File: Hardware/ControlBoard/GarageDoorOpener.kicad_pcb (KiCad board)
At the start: 2 copper layers, 24 parts, among them J1 Conn_01x02, J2 Conn_01x02, J3 Conn_01x02, J4 Conn_01x02, Q1 DMG1012T-7, U1 RAC15-05SK, U2 CPC1002N

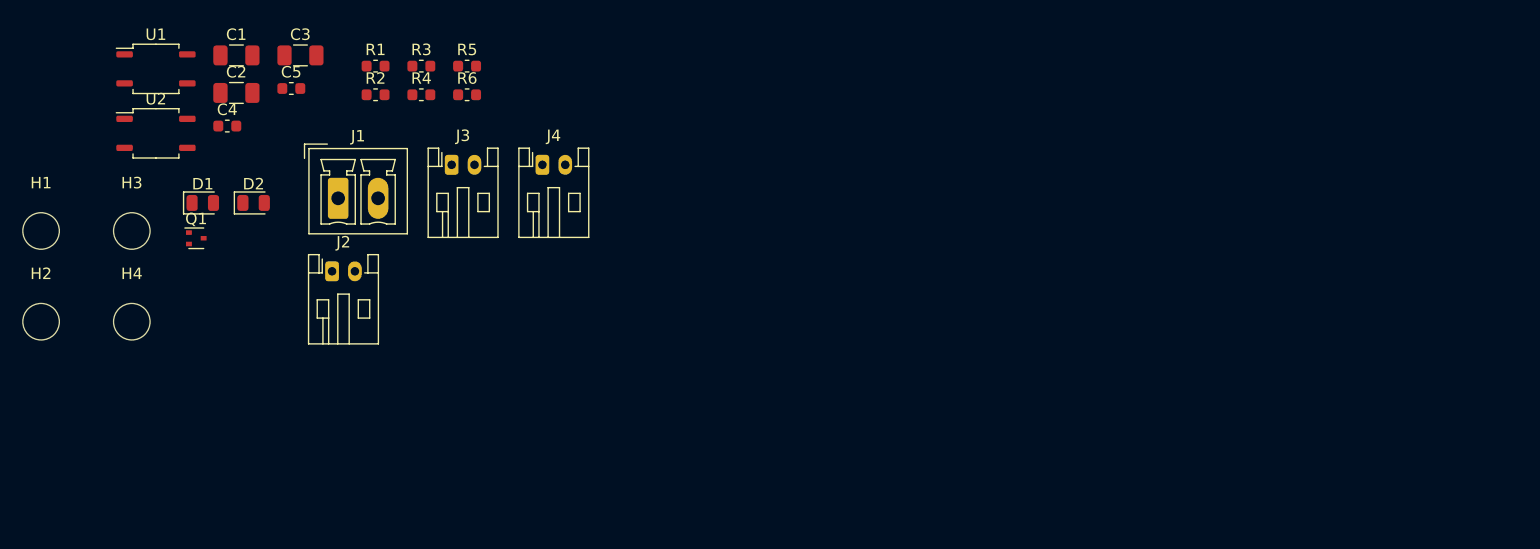
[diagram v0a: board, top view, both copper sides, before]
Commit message: Schematics done, PCBs have components dropped in and BoM finished
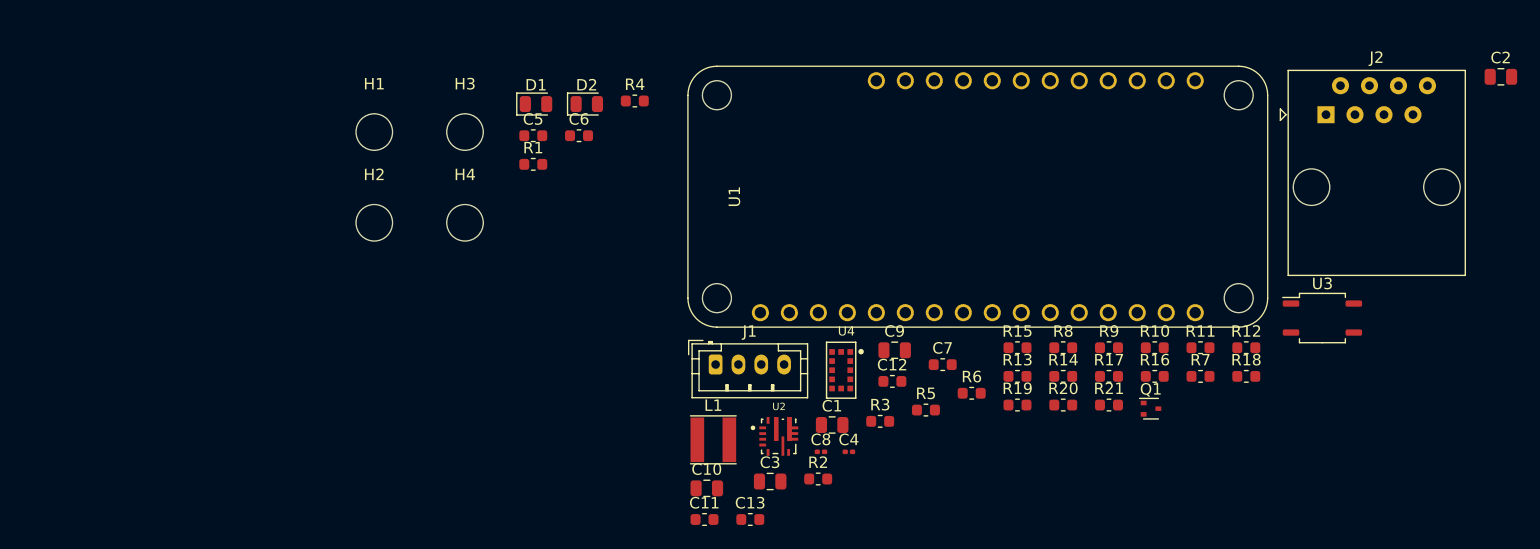
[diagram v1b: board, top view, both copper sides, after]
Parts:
- removed J3, J4: Conn_01x02, Connector_JST:JST_PH_S2B-PH-K_1x02_P2.00mm_Horizontal
- added C10: 22uF 10V, Capacitor_SMD:C_0805_2012Metric, F.Cu at (201.1, 131.0)
- added C11: 4.7uF 10V, Capacitor_SMD:C_0603_1608Metric, F.Cu at (200.9, 133.7)
- added C12: 0.1uF 16V, Capacitor_SMD:C_0603_1608Metric, F.Cu at (217.3, 121.6)
- added C13: 4.7uF 10V, Capacitor_SMD:C_0603_1608Metric, F.Cu at (204.9, 133.7)
- added C6: 1uF 10V, Capacitor_SMD:C_0603_1608Metric, F.Cu at (189.9, 100.1)
- added C7: 0.1uF 16V, Capacitor_SMD:C_0603_1608Metric, F.Cu at (221.8, 120.2)
- added C8: 100pF 10V, Capacitor_SMD:C_0201_0603Metric, F.Cu at (211.1, 127.8)
- added C9: 22uF 10V, Capacitor_SMD:C_0805_2012Metric, F.Cu at (217.5, 118.9)
- added L1: 3.3uH, Inductor_SMD:L_Taiyo-Yuden_NR-40xx, F.Cu at (201.7, 126.8)
- added R10: 73.2K, Resistor_SMD:R_0603_1608Metric, F.Cu at (240.3, 118.7)
- added R11: 10K, Resistor_SMD:R_0603_1608Metric, F.Cu at (244.3, 118.7)
- added R12: 4.7K, Resistor_SMD:R_0603_1608Metric, F.Cu at (248.4, 118.7)
- added R13: 4.7K, Resistor_SMD:R_0603_1608Metric, F.Cu at (228.3, 121.2)
- added R14: 10K, Resistor_SMD:R_0603_1608Metric, F.Cu at (232.3, 121.2)
- added R15: 10K, Resistor_SMD:R_0603_1608Metric, F.Cu at (228.3, 118.7)
- added R16: 0, Resistor_SMD:R_0603_1608Metric, F.Cu at (240.3, 121.2)
- added R17: 0, Resistor_SMD:R_0603_1608Metric, F.Cu at (236.3, 121.2)
- added R18: 0, Resistor_SMD:R_0603_1608Metric, F.Cu at (248.4, 121.2)
- added R19: 0, Resistor_SMD:R_0603_1608Metric, F.Cu at (228.3, 123.7)
- added R20: 0, Resistor_SMD:R_0603_1608Metric, F.Cu at (232.3, 123.7)
- added R21: 0, Resistor_SMD:R_0603_1608Metric, F.Cu at (236.3, 123.7)
- added R7: 10K, Resistor_SMD:R_0603_1608Metric, F.Cu at (244.3, 121.2)
- added R8: 20K, Resistor_SMD:R_0603_1608Metric, F.Cu at (232.3, 118.7)
- added R9: 10K, Resistor_SMD:R_0603_1608Metric, F.Cu at (236.3, 118.7)
- added U3: CPC1002N, Package_SO:SOP-4_3.8x4.1mm_P2.54mm, F.Cu at (255.0, 116.1)
- added U4: VL53L1X, Global_Parts:VL53L1CXV0FY_1, F.Cu at (212.9, 120.7)
- C1, C2, C3: value 47uF 10V -> 4.7uF 50V; footprint Capacitor_SMD:C_1206_3216Metric -> Capacitor_SMD:C_0805_2012Metric
- C4: value 1uF 10V -> 0.1uF 50V; footprint Capacitor_SMD:C_0603_1608Metric -> Capacitor_SMD:C_0201_0603Metric
- D1: value LED -> GREEN_LED
- D2: value LED -> RED_LED
- J1: value Conn_01x02 -> Conn_01x04; footprint Connector_Phoenix_MC:PhoenixContact_MCV_1,5_2-G-3.5_1x02_P3.50mm_Vertical -> Connector_JST:JST_PH_B4B-PH-K_1x04_P2.00mm_Vertical
- J2: value Conn_01x02 -> RJ45; footprint Connector_JST:JST_PH_S2B-PH-K_1x02_P2.00mm_Horizontal -> Connector_RJ:RJ45_Amphenol_54602-x08_Horizontal
- R1: value 1K -> 649
- R2: value 1K -> 10K
- R3: value 10K -> 649
- R4: value 649 -> 1K
- U1: value RAC15-05SK -> Argon/Boron; footprint Package_SO:SOP-4_3.8x4.1mm_P2.54mm -> Global_Parts:ParticleBoron
- U2: value CPC1002N -> TPS56637; footprint Package_SO:SOP-4_3.8x4.1mm_P2.54mm -> Global_Parts:TPS56637RPAR
- moved C2 110.8 mm to (270.7, 94.9)
- moved J2 88.2 mm to (255.3, 98.3)
- moved Q1 85.0 mm to (240.0, 124.0)
- moved U1 70.4 mm to (222.3, 105.4)
- moved C4 61.5 mm to (213.5, 127.8)
- moved C1 61.4 mm to (212.1, 125.5)
- moved U2 60.7 mm to (207.4, 126.5)
- moved C3 55.6 mm to (206.6, 130.4)
- moved R6 51.4 mm to (224.3, 122.7)
- moved R2 51.4 mm to (210.8, 130.2)
- moved R3 50.8 mm to (216.3, 125.1)
- moved R5 50.2 mm to (220.3, 124.1)
- moved J1 36.1 mm to (201.9, 120.2)
- moved D2 30.5 mm to (190.6, 97.3)
- moved D1 30.5 mm to (186.1, 97.3)
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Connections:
- C1 pad 1: +5V -> +24V
- C2 pad 1: +5V -> +24V
- C3 pad 1: +5V -> +24V
- C4 pad 1: +3V3 -> +24V
- J1 pad 1: Net-(J1-Pad1) -> +5V
- J1 pad 2: Net-(J1-Pad2) -> /LED_STRIP_CLK
- J2 pad 1: Net-(J2-Pad1) -> +24V
- J2 pad 2: Net-(J2-Pad2) -> GND
- Q1 pad 1: /RELAY_CTRL -> /RELAY_CTRL1
- R2 pad 1: /STATUS_LED -> GND
- R2 pad 2: Net-(D2-Pad2) -> /RELAY_CTRL1
- R3 pad 1: GND -> Net-(R3-Pad1)
- R3 pad 2: /RELAY_CTRL -> +3V3
- R4 pad 1: Net-(R4-Pad1) -> /STATUS_LED
- R4 pad 2: +3V3 -> Net-(D2-Pad2)
- R5 pad 1: +3V3 -> +24V
- R5 pad 2: /REED_SW1 -> Net-(R5-Pad2)
- R6 pad 1: +3V3 -> +5V
- R6 pad 2: /REED_SW2 -> Net-(R6-Pad2)
- U1 pad 1: Net-(J1-Pad1) -> Net-(U1-Pad1)
- U1 pad 2: (no net) -> +3V3
- U1 pad 3: (no net) -> Net-(U1-Pad3)
- U1 pad 4: (no net) -> GND
- U2 pad 1: Net-(R4-Pad1) -> Net-(R5-Pad2)
- U2 pad 2: Net-(Q1-Pad3) -> Net-(C8-Pad1)
- U2 pad 3: Net-(J2-Pad2) -> GND
- U2 pad 4: Net-(J2-Pad1) -> Net-(R6-Pad2)

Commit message: working on the PCB for the control board
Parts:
- C4, C8: footprint Capacitor_SMD:C_0201_0603Metric -> Capacitor_SMD:C_0603_1608Metric
- moved C2 160.3 mm to (110.6, 85.6), turned to 180 degrees
- moved J2 160.2 mm to (98.2, 66.9), turned to 270 degrees
- moved R18 150.8 mm to (105.7, 72.4)
- moved R16 144.3 mm to (105.7, 69.3)
- moved U3 142.2 mm to (120.6, 69.6), turned to 180 degrees
- moved R11 139.0 mm to (107.3, 95.7), turned to 270 degrees
- moved R17 137.0 mm to (108.9, 70.9)
- moved R21 135.7 mm to (108.9, 77.0)
- moved R20 135.5 mm to (105.7, 75.4)
- moved R10 134.5 mm to (107.3, 98.9), turned to 270 degrees
- moved R19 129.3 mm to (108.9, 73.9)
- moved R8 128.3 mm to (105.6, 98.9), turned to 270 degrees
- moved Q1 127.1 mm to (125.8, 68.3), turned to 180 degrees
- moved R6 117.9 mm to (109.7, 94.8), turned to 180 degrees
- moved R12 117.9 mm to (130.5, 116.0)
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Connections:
- U3 pad 3: /Relay_Ouput2 -> /Relay_Ouput1
- U3 pad 4: /Relay_Ouput1 -> /Relay_Ouput2
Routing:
- net /Relay_Ouput1: track 0.00 -> 11.8 mm
- net /Relay_Ouput2: track 0.00 -> 8.12 mm
- net Net-(J2-Pad8): track 0.00 -> 7.88 mm
- net Net-(J2-Pad6): track 0.00 -> 7.66 mm
- net Net-(J2-Pad4): track 0.00 -> 7.45 mm
- net Net-(J2-Pad7): track 0.00 -> 7.03 mm
- net Net-(J2-Pad5): track 0.00 -> 6.82 mm
- net Net-(J2-Pad3): track 0.00 -> 6.70 mm
- net +3V3: track 0.00 -> 6.50 mm
- net /SENSOR_SHUTDOWN: track 0.00 -> 3.94 mm
- net +5V: track 0.00 -> 3.64 mm
- net /SENSOR_INT: track 0.00 -> 3.18 mm
- net /SENSOR_I2C_SCL: track 0.00 -> 2.36 mm
- net /SENSOR_I2C_SDA: track 0.00 -> 2.35 mm
- net Net-(R3-Pad1): track 0.00 -> 1.86 mm
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
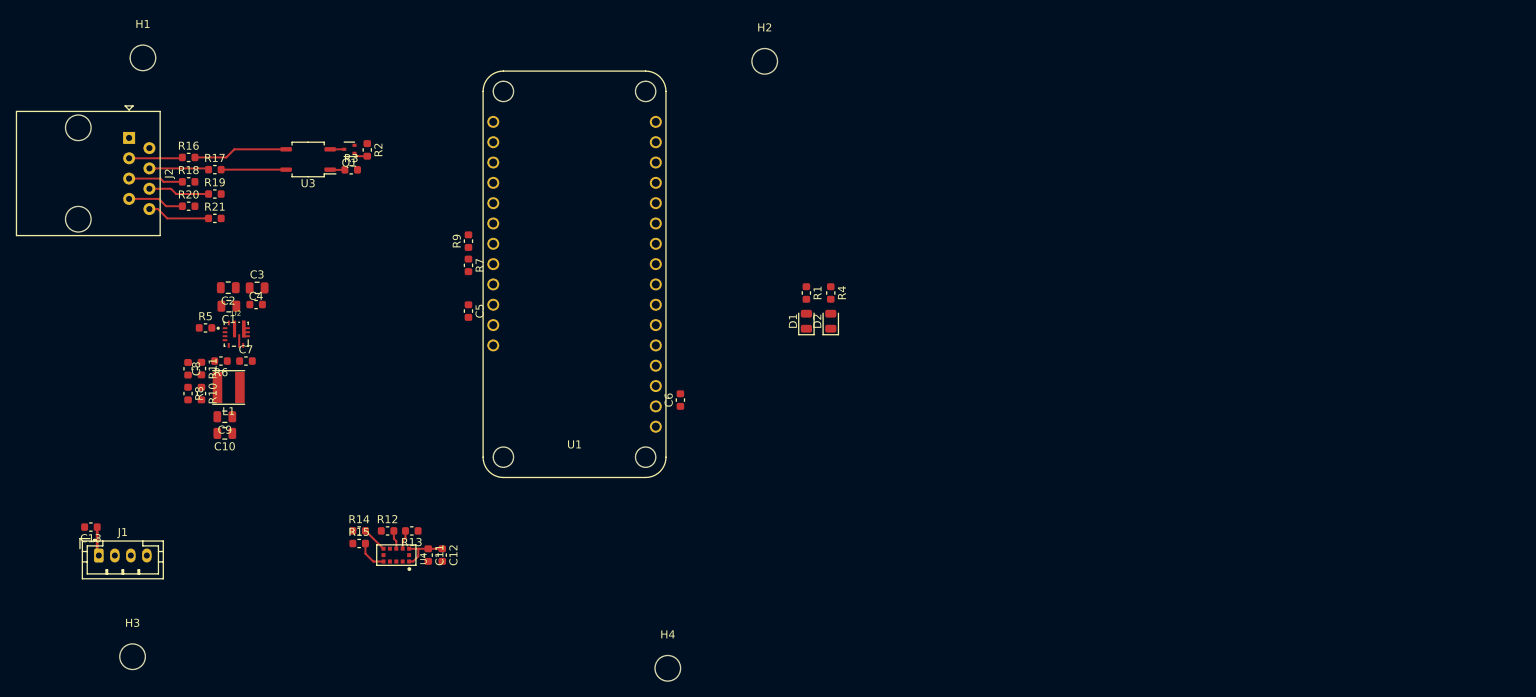
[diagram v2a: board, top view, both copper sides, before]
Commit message: placement of components 80% board outline done
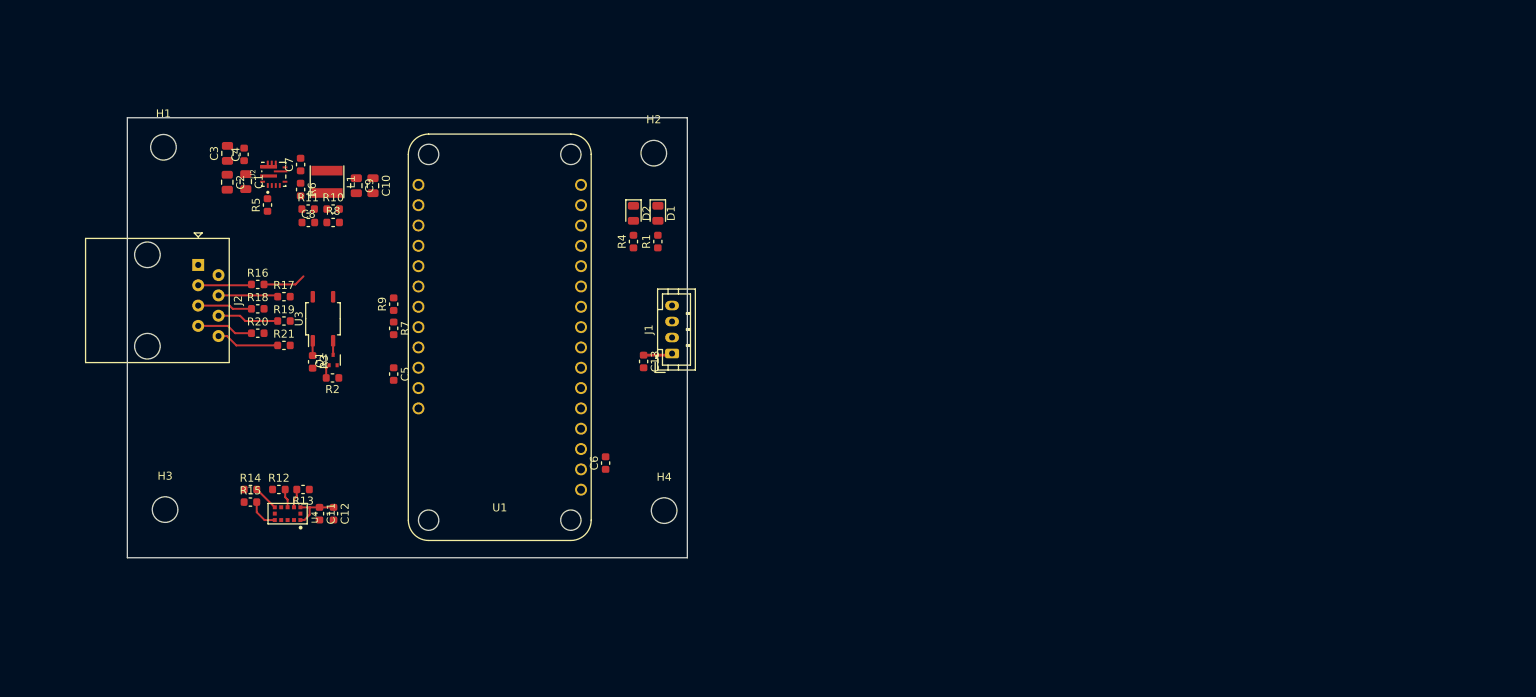
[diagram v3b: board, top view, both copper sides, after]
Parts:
- moved J1 76.0 mm to (166.1, 93.9), turned to 90 degrees
- moved C13 72.1 mm to (162.5, 94.8), turned to 270 degrees
- moved C10 36.1 mm to (128.7, 72.9), turned to 270 degrees
- moved C9 33.2 mm to (126.6, 72.9), turned to 270 degrees
- moved R2 28.8 mm to (123.6, 96.9), turned to 180 degrees
- moved L1 28.5 mm to (123.0, 72.4), turned to 270 degrees
- moved R10 28.3 mm to (123.7, 75.8), turned to 0 degrees
- moved D2 28.1 mm to (161.3, 76.3), turned to 270 degrees
- moved R8 28.0 mm to (123.7, 77.5), turned to 0 degrees
- moved Q1 26.4 mm to (123.7, 94.7), turned to 90 degrees
- moved C7 25.5 mm to (119.7, 70.2), turned to 90 degrees
- moved R4 25.5 mm to (161.3, 79.9), turned to 90 degrees
- moved R3 24.5 mm to (121.2, 94.9), turned to 270 degrees
- moved R11 24.0 mm to (120.6, 75.8), turned to 0 degrees
- moved C8 23.7 mm to (120.6, 77.5), turned to 0 degrees
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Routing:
- net /Relay_Ouput2: track 8.12 -> 0.00 mm
- net /Relay_Ouput1: track 11.8 -> 5.35 mm
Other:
- board outline added: 70 x 55 mm

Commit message: first pass of completed control board done
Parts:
- moved C3 5.25 mm to (110.9, 74.1)
- moved C1 5.15 mm to (113.2, 77.5)
- moved C2 5.15 mm to (110.9, 77.6)
- moved C8 5.15 mm to (121.0, 82.6)
- moved R10 5.15 mm to (124.1, 80.9)
- moved R11 5.15 mm to (121.0, 80.9)
- moved R8 5.15 mm to (124.1, 82.6)
- moved C4 5.15 mm to (113.0, 74.1)
- moved C7 5.15 mm to (120.1, 75.4)
- moved R6 5.15 mm to (120.1, 78.5)
- moved U2 5.15 mm to (116.7, 76.6)
- moved C10 5.15 mm to (129.1, 78.0)
- moved C9 5.15 mm to (127.0, 78.0)
- moved J2 5.11 mm to (109.1, 87.4)
- moved L1 5.02 mm to (123.4, 77.4)
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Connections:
- R19 pad 2: /REED_SW2_GND -> GND
- R21 pad 2: /REED_SW1_GND -> GND
- R7 pad 2: /REED_SW1 -> /REED_SW1_IN
- R9 pad 2: /REED_SW2 -> /REED_SW2_IN
- U1 pad 23: /REED_SW2 -> /REED_SW2_IN
- U1 pad 24: /REED_SW1 -> /REED_SW1_IN
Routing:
- net +3V3: track 6.50 -> 109.1 mm, vias 0 -> 5
- net /SENSOR_I2C_SDA: track 2.35 -> 55.4 mm
- net +5V: track 3.64 -> 56.0 mm, vias 0 -> 2
- net /SENSOR_INT: track 3.18 -> 52.5 mm
- net /SENSOR_SHUTDOWN: track 3.94 -> 53.1 mm
- net /SENSOR_I2C_SCL: track 2.36 -> 50.7 mm
- net +24V: track 0.00 -> 28.3 mm
- net /STATUS_LED: track 0.00 -> 23.8 mm
- net /CONNECTIVITY_LED: track 0.00 -> 21.4 mm
- net /REED_SW2_IN: track 0.00 -> 21.3 mm
- net /REED_SW1_IN: track 0.00 -> 18.7 mm
- net /LED_STRIP_DATA: track 0.00 -> 14.1 mm
- net /LED_STRIP_CLK: track 0.00 -> 13.8 mm
- net /RELAY_CTRL1: track 1.74 -> 12.6 mm
- net Net-(C8-Pad1): track 0.00 -> 10.7 mm
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- added copper zone on F.Cu, net +24V
- added copper zone on F.Cu, net +5V
- added copper zone on B.Cu, net GND
- added copper zone on F.Cu, net GND
- added copper zone on F.Cu, net Net-(C7-Pad1)
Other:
- board size 70 x 55 mm -> 70 x 52 mm

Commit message: minor tweaks as I was making a readme
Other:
- board text added: "Martian Engineering Matthew Glazer Garage Door Control Board Rev1b"
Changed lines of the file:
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@@
   (general
     (thickness 1.6)
-    (drawings 4)
+    (drawings 5)
     (tracks 281)
     (zones 0)
@@
     (title "Garage Door Control Board")
     (date 2020-05-10)
-    (rev 1a)
+    (rev 1b)
     (company "MARTIAN ENGINEERING")
     (comment 1 "Designer: Matthew Glazer")
@@
     (pad 1 smd rect (at -1.4 0 270) (size 1.2 3.9) (layers F.Cu F.Paste F.Mask)
       (net 11 "Net-(C7-Pad1)"))
-    (model ${KISYS3DMOD}/Inductor_SMD.3dshapes/L_Taiyo-Yuden_NR-40xx.wrl
-      (at (xyz 0 0 0))
-      (scale (xyz 1 1 1))
+    (model ${KISYS3DMOD}/Inductors_SMD.3dshapes/L_Wuerth_MAPI-1610.step
+      (at (xyz 0 0 0))
+      (scale (xyz 2.5 2.5 2.5))
       (rotate (xyz 0 0 0))
     )
@@
       (scale (xyz 1 1 1))
       (rotate (xyz 0 0 0))
+    )
+    (model ${KISYS3DMOD}/Connector_RJ.3dshapes/RJ45_Amphenol_RJHSE538X.step
+      (offset (xyz 7.5 -5.5 0.5))
+      (scale (xyz 0.9 1.1 0.9))
+      (rotate (xyz 0 0 -180))
     )
   )
@@
       (rotate (xyz 0 0 0))
     )
+  )
+  (gr_text "Martian Engineering\nMatthew Glazer\nGarage Door Control Board Rev1b" (at 106.553 115.4684) (layer F.SilkS)
+    (effects (font (size 1 1) (thickness 0.15)) (justify left))
   )
   (gr_line (start 98 67.38) (end 168 67.38) (layer Edge.Cuts) (width 0.05))
@@
   (segment (start 152.1714 82.55) (end 153.703601 81.017799) (width 0.25) (layer F.Cu) (net 8))
   (segment (start 157.192399 81.017799) (end 159.7661 83.5915) (width 0.25) (layer F.Cu) (net 8))
-  (segment (start 132.0545 92.2528) (end 131.2926 91.4909) (width 0.25) (layer F.Cu) (net 33))
-  (segment (start 134.5184 92.2528) (end 132.0545 92.2528) (width 0.25) (layer F.Cu) (net 33))
-  (segment (start 131.3687 86.8933) (end 131.2926 86.8933) (width 0.25) (layer F.Cu) (net 32))
-  (segment (start 134.5184 89.7128) (end 134.1882 89.7128) (width 0.25) (layer F.Cu) (net 32))
-  (segment (start 134.1882 89.7128) (end 131.3687 86.8933) (width 0.25) (layer F.Cu) (net 32))
   (segment (start 113.3188 75.631) (end 113.0046 75.3168) (width 0.25) (layer F.Cu) (net 9))
   (segment (start 113.0046 75.3168) (end 113.0046 74.8793) (width 0.25) (layer F.Cu) (net 9))
@@
   (segment (start 123.8572 90.9066) (end 123.8758 90.9252) (width 0.25) (layer F.Cu) (net 31))
   (segment (start 121.0565 90.9066) (end 123.8572 90.9066) (width 0.25) (layer F.Cu) (net 31))
+  (segment (start 131.3687 86.8933) (end 131.2926 86.8933) (width 0.25) (layer F.Cu) (net 32))
+  (segment (start 134.5184 89.7128) (end 134.1882 89.7128) (width 0.25) (layer F.Cu) (net 32))
+  (segment (start 134.1882 89.7128) (end 131.3687 86.8933) (width 0.25) (layer F.Cu) (net 32))
   (segment (start 131.2419 86.8933) (end 131.2926 86.8933) (width 0.25) (layer F.Cu) (net 32))
   (segment (start 128.3716 91.567) (end 128.3716 89.7636) (width 0.25) (layer F.Cu) (net 32))
@@
   (segment (start 117.7799 92.4306) (end 127.508 92.4306) (width 0.25) (layer F.Cu) (net 32))
   (segment (start 127.508 92.4306) (end 128.3716 91.567) (width 0.25) (layer F.Cu) (net 32))
+  (segment (start 132.0545 92.2528) (end 131.2926 91.4909) (width 0.25) (layer F.Cu) (net 33))
+  (segment (start 134.5184 92.2528) (end 132.0545 92.2528) (width 0.25) (layer F.Cu) (net 33))
   (segment (start 131.2417 91.4909) (end 131.2926 91.4909) (width 0.25) (layer F.Cu) (net 33))
   (segment (start 128.651 94.0816) (end 131.2417 91.4909) (width 0.25) (layer F.Cu) (net 33))
